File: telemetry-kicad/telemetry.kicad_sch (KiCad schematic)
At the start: 98 parts, among them J1 2601-1102, J2 RFPC-SMA27-F, J3 TC2030, J4 2601-1102, J5 2601-1102, J6 USB_C_Receptacle_USB2.0_16P, J7 SD_Card_Receptacle, Q1 DMP3099LQ-7, SW1 SW_NRST, SW2 SW_BOOT0, U1 LMR33610ADDAR, U10 TLC59108IPWR, U11 MCP1703T-5002E/CB, U2 ASM330LHHXG1TR, U3 MAX-M10S-00B, U4 TCAN337, U5 STM32H523RCT7, U6 TCAN337, U7 USBLC6-2SC6, U9 TLC59108IPWR, Y1 ABM8AIG-24.000MHz-8-2Z-T

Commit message: PCB draft complete
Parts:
- removed C28: 1uF, Capacitor_SMD:C_0805_2012Metric_Pad1.18x1.45mm_HandSolder, symbol Device:C
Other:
- moved on the sheet: C26, C27
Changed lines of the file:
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@@
 	(text "VDD (with bulk) and VDD_IO"
 		(exclude_from_sim no)
-		(at 130.048 257.302 0)
+		(at 130.048 258.572 0)
 		(effects
 			(font
@@
 	)
 	(junction
+		(at 139.7 252.73)
+		(diameter 0)
+		(color 0 0 0 0)
+	)
+	(junction
 		(at 57.15 41.91)
 		(diameter 0)
@@
 	)
 	(junction
-		(at 186.69 252.73)
+		(at 139.7 240.03)
 		(diameter 0)
 		(color 0 0 0 0)
 	)
 	(junction
-		(at 422.91 113.03)
+		(at 186.69 252.73)
 		(diameter 0)
 		(color 0 0 0 0)
 	)
 	(junction
-		(at 232.41 237.49)
+		(at 422.91 113.03)
 		(diameter 0)
 		(color 0 0 0 0)
 	)
 	(junction
-		(at 93.98 31.75)
+		(at 232.41 237.49)
 		(diameter 0)
 		(color 0 0 0 0)
 	)
 	(junction
-		(at 140.97 240.03)
+		(at 93.98 31.75)
 		(diameter 0)
 		(color 0 0 0 0)
@@
 	)
 	(junction
-		(at 140.97 252.73)
-		(diameter 0)
-		(color 0 0 0 0)
-	)
-	(junction
 		(at 186.69 240.03)
 		(diameter 0)
@@
 	(wire
 		(pts
-			(xy 153.67 240.03) (xy 153.67 242.57)
-		)
-		(stroke
-			(width 0)
-			(type default)
-		)
-	)
-	(wire
-		(pts
 			(xy 172.72 124.46) (xy 172.72 119.38)
 		)
@@
 	(wire
 		(pts
-			(xy 140.97 237.49) (xy 140.97 240.03)
+			(xy 139.7 238.76) (xy 139.7 240.03)
 		)
 		(stroke
@@
 	(wire
 		(pts
-			(xy 140.97 250.19) (xy 140.97 252.73)
+			(xy 146.05 250.19) (xy 146.05 252.73)
 		)
 		(stroke
@@
 	(wire
 		(pts
-			(xy 140.97 240.03) (xy 140.97 242.57)
-		)
-		(stroke
-			(width 0)
-			(type default)
-		)
-	)
-	(wire
-		(pts
-			(xy 153.67 252.73) (xy 153.67 250.19)
+			(xy 146.05 240.03) (xy 146.05 242.57)
 		)
 		(stroke
@@
 	(wire
 		(pts
-			(xy 140.97 240.03) (xy 153.67 240.03)
-		)
-		(stroke
-			(width 0)
-			(type default)
-		)
-	)
-	(wire
-		(pts
 			(xy 194.31 172.72) (xy 195.58 172.72)
 		)
@@
 	(wire
 		(pts
-			(xy 127 240.03) (xy 140.97 240.03)
+			(xy 132.08 240.03) (xy 139.7 240.03)
 		)
 		(stroke
@@
 	(wire
 		(pts
-			(xy 127 250.19) (xy 127 252.73)
+			(xy 132.08 250.19) (xy 132.08 252.73)
 		)
 		(stroke
@@
 	(wire
 		(pts
-			(xy 127 242.57) (xy 127 240.03)
+			(xy 132.08 242.57) (xy 132.08 240.03)
 		)
 		(stroke
@@
 	(wire
 		(pts
-			(xy 140.97 252.73) (xy 153.67 252.73)
-		)
-		(stroke
-			(width 0)
-			(type default)
-		)
-	)
-	(wire
-		(pts
 			(xy 124.46 114.3) (xy 123.19 114.3)
 		)
@@
 	(wire
 		(pts
+			(xy 139.7 240.03) (xy 146.05 240.03)
+		)
+		(stroke
+			(width 0)
+			(type default)
+		)
+	)
+	(wire
+		(pts
+			(xy 139.7 252.73) (xy 146.05 252.73)
+		)
+		(stroke
+			(width 0)
+			(type default)
+		)
+	)
+	(wire
+		(pts
 			(xy 238.76 39.37) (xy 238.76 34.29)
 		)
@@
 	(wire
 		(pts
-			(xy 127 252.73) (xy 140.97 252.73)
+			(xy 132.08 252.73) (xy 139.7 252.73)
 		)
 		(stroke
@@
 	(wire
 		(pts
-			(xy 140.97 252.73) (xy 140.97 255.27)
+			(xy 139.7 252.73) (xy 139.7 254)
 		)
 		(stroke
@@
 	(symbol
 		(lib_id "Device:C")
-		(at 140.97 246.38 0)
+		(at 146.05 246.38 0)
 		(unit 1)
 		(body_style 1)
@@
 		(fields_autoplaced yes)
 		(property "Reference" "C27"
-			(at 144.78 245.1099 0)
+			(at 149.86 245.1099 0)
 			(show_name no)
 			(do_not_autoplace no)
@@
 		)
 		(property "Value" "1uF"
-			(at 144.78 247.6499 0)
+			(at 149.86 247.6499 0)
 			(show_name no)
 			(do_not_autoplace no)
@@
 		)
 		(property "Footprint" "Capacitor_SMD:C_0805_2012Metric_Pad1.18x1.45mm_HandSolder"
-			(at 141.9352 250.19 0)
+			(at 147.0152 250.19 0)
 			(hide yes)
 			(show_name no)
@@
 		)
 		(property "Datasheet" ""
-			(at 140.97 246.38 0)
+			(at 146.05 246.38 0)
 			(hide yes)
 			(show_name no)
@@
 		)
 		(property "Description" "Unpolarized capacitor"
-			(at 140.97 246.38 0)
+			(at 146.05 246.38 0)
 			(hide yes)
 			(show_name no)
@@
 	(symbol
 		(lib_id "power:+3.3V")
-		(at 140.97 237.49 0)
+		(at 139.7 238.76 0)
 		(unit 1)
 		(body_style 1)
@@
 		(fields_autoplaced yes)
 		(property "Reference" "#PWR076"
-			(at 140.97 241.3 0)
+			(at 139.7 242.57 0)
 			(hide yes)
 			(show_name no)
@@
 		)
 		(property "Value" "+3.3V"
-			(at 140.97 232.41 0)
+			(at 139.7 233.68 0)
 			(show_name no)
 			(do_not_autoplace no)
@@
 		)
 		(property "Footprint" ""
-			(at 140.97 237.49 0)
+			(at 139.7 238.76 0)
 			(hide yes)
 			(show_name no)
@@
 		)
 		(property "Datasheet" ""
-			(at 140.97 237.49 0)
+			(at 139.7 238.76 0)
 			(hide yes)
 			(show_name no)
@@
 		)
 		(property "Description" "Power symbol creates a global label with name \"+3.3V\""
-			(at 140.97 237.49 0)
+			(at 139.7 238.76 0)
 			(hide yes)
 			(show_name no)
@@
 	(symbol
 		(lib_id "Device:C")
-		(at 127 246.38 180)
+		(at 132.08 246.38 180)
 		(unit 1)
 		(body_style 1)
@@
 		(fields_autoplaced yes)
 		(property "Reference" "C26"
-			(at 130.81 245.1099 0)
+			(at 135.89 245.1099 0)
 			(show_name no)
 			(do_not_autoplace no)
@@
 		)
 		(property "Value" "10uF"
-			(at 130.81 247.6499 0)
+			(at 135.89 247.6499 0)
 			(show_name no)
 			(do_not_autoplace no)
@@
 		)
 		(property "Footprint" "Capacitor_SMD:C_0805_2012Metric_Pad1.18x1.45mm_HandSolder"
-			(at 126.0348 242.57 0)
+			(at 131.1148 242.57 0)
 			(hide yes)
 			(show_name no)
@@
 		)
 		(property "Datasheet" ""
-			(at 127 246.38 0)
+			(at 132.08 246.38 0)
 			(hide yes)
 			(show_name no)
@@
 		)
 		(property "Description" "Unpolarized capacitor"
-			(at 127 246.38 0)
+			(at 132.08 246.38 0)
 			(hide yes)
 			(show_name no)
@@
 	(symbol
 		(lib_id "power:GND")
-		(at 140.97 255.27 0)
+		(at 139.7 254 0)
 		(unit 1)
 		(body_style 1)
@@
 		(fields_autoplaced yes)
 		(property "Reference" "#PWR081"
-			(at 140.97 261.62 0)
+			(at 139.7 260.35 0)
 			(hide yes)
 			(show_name no)
@@
 		)
 		(property "Value" "GND"
-			(at 140.97 260.35 0)
+			(at 139.7 259.08 0)
 			(hide yes)
 			(show_name no)
@@
 		)
 		(property "Footprint" ""
-			(at 140.97 255.27 0)
+			(at 139.7 254 0)
 			(hide yes)
 			(show_name no)
@@
 		)
 		(property "Datasheet" ""
-			(at 140.97 255.27 0)
+			(at 139.7 254 0)
 			(hide yes)
 			(show_name no)
@@
 		)
 		(property "Description" "Power symbol creates a global label with name \"GND\" , ground"
-			(at 140.97 255.27 0)
+			(at 139.7 254 0)
 			(hide yes)
 			(show_name no)
@@
 					(unit 1)
 				)
-			)
-		)
-	)
-	(symbol
-		(lib_id "Device:C")
-		(at 153.67 246.38 0)
-		(unit 1)
-		(body_style 1)
-		(exclude_from_sim no)
-		(in_bom yes)
-		(on_board yes)
-		(in_pos_files yes)
-		(dnp no)
-		(fields_autoplaced yes)
-		(property "Reference" "C28"
-			(at 157.48 245.1099 0)
-			(show_name no)
-			(do_not_autoplace no)
-			(effects
-				(font
-					(size 1.27 1.27)
-				)
-				(justify left)
-			)
-		)
-		(property "Value" "1uF"
-			(at 157.48 247.6499 0)
-			(show_name no)
-			(do_not_autoplace no)
-			(effects
-				(font
-					(size 1.27 1.27)
-				)
-				(justify left)
-			)
-		)
-		(property "Footprint" "Capacitor_SMD:C_0805_2012Metric_Pad1.18x1.45mm_HandSolder"
-			(at 154.6352 250.19 0)
-			(hide yes)
-			(show_name no)
-			(do_not_autoplace no)
-			(effects
-				(font
-					(size 1.27 1.27)
-				)
-			)
-		)
-		(property "Datasheet" ""
-			(at 153.67 246.38 0)
-			(hide yes)
-			(show_name no)
-			(do_not_autoplace no)
-			(effects
-				(font
-					(size 1.27 1.27)
-				)
-			)
-		)
-		(property "Description" "Unpolarized capacitor"
-			(at 153.67 246.38 0)
-			(hide yes)
-			(show_name no)
-			(do_not_autoplace no)
-			(effects
-				(font
-					(size 1.27 1.27)
-				)
-			)
-		)
-		(pin "1"
-		)
-		(pin "2"
-		)
-		(instances
-			(project "telemetry"
-				(path "/3df6834d-aaf5-42e5-8a41-0f444a5b1186"
-					(reference "C28")
-					(unit 1)
-				)

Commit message: Changed ublox MAX-M10 to Quectel LC29HBAMD to enable the option of using RTK as well as keeping the dead reckoning features
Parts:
- removed U3: MAX-M10S-00B, telemetry:MAX-M10S-00B, symbol telemetry:MAX-M10S-00B
- added R22: 10K, Resistor_SMD:R_0805_2012Metric_Pad1.20x1.40mm_HandSolder, symbol Device:R_US
- added R23: 39k, LC29HBAMD, symbol Device:R_US
- added SW3: CJS-1200TB1, bspd:CJS-1200TB1, symbol telemetry:CJS-1200TB1
- added U3: LC29HBAMD, LC29HBAMD, symbol telemetry:LC29HBAMD
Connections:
- net +3.3V: now also C33.2, C34.2, U10.20 (VCC), U9.20 (VCC), R22.1, U3.22 (V_BCKP), U3.23 (VCC)
- net +5V: no longer C33.2, C34.2, U10.20 (VCC), U9.20 (VCC)
- net ANT: now also U3.11 (RF_IN)
- net CS_IMU: now also R22.2
- net GND: now also U3.10 (GND), U3.12 (GND), U3.13 (GND), U3.24 (GND)
- net RXD_CAN2: now also U5.33 (PB12); no longer U5.34 (PB13)
- net TXD_CAN2: now also U5.34 (PB13); no longer U5.33 (PB12)
- net VBUS_USB: now also C32.2, D6.1 (K), U11.3 (VIN)
- net V_IN: no longer C32.2, D6.1 (K), U11.3 (VIN)
- net RXD_GNSS: no longer names the net of U5.35 (PB14)
- net TXD_GNSS: no longer names the net of U5.36 (PB15)
- new net: R23.1, U3.7 (VDD_EXT)
- new net: R23.2, U3.5 (D_SEL1)
- new net CLK_GNSS: U3.19 (I2C_SCL/SPI_CLK)
- new net CS_GNSS: U3.18 (I2C_SDA/SPI_CS)
- new net MISO_GNSS: U3.20 (TXD1/SPI_MISO)
- new net MOSI_GNSS: U3.21 (RXD1/SPI_MOSI)
- new net RESET_GNSS: U3.8 (RESET_IN)
- new net TIMERIN_GNSS: U3.3 (1PPS)
- no-connect marks 13 -> 5
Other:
- note added: "Level shifting required for a bunch of things"
- moved on the sheet: C11, J2

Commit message: update
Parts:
- R23, U3: footprint LC29HBAMD -> (none)
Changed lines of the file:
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@@
 			)
 		)
-		(property "Footprint" "LC29HBAMD"
+		(property "Footprint" ""
 			(at 29.464 89.154 90)
 			(hide yes)
@@
 			)
 		)
-		(property "Footprint" "LC29HBAMD"
+		(property "Footprint" ""
 			(at 40.64 74.93 0)
 			(hide yes)

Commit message: Added 12V/USB_5V power mux and level shifting for GNSS module
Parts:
- added C28, C36, C38: 100nF, Capacitor_SMD:C_0805_2012Metric_Pad1.18x1.45mm_HandSolder, symbol Device:C
- added C37: 10uF, Capacitor_SMD:C_0805_2012Metric_Pad1.18x1.45mm_HandSolder, symbol Device:C
- added C39: 1uF, Capacitor_SMD:C_0805_2012Metric_Pad1.18x1.45mm_HandSolder, symbol Device:C
- added R24: 10k, Resistor_SMD:R_0805_2012Metric_Pad1.20x1.40mm_HandSolder, symbol Device:R_US
- added R25, R26, R29, R30: R_US, Resistor_THT:R_Array_SIP4, symbol Device:R_US
- added R31: 21.5k, Resistor_THT:R_Array_SIP4, symbol Device:R_US
- added U13: TXS0108EPW, Package_SO:TSSOP-20_4.4x6.5mm_P0.65mm, symbol Logic_LevelTranslator:TXS0108EPW
- added U8: TPS2121RUXR, telemetry:VQFN-HR-12_L2.5-W2.0-P0.50-BL, symbol telemetry:TPS2121RUXR
- U3: footprint (none) -> LC29HBAMD
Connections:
- net TIMEPULSE_GNSS is gone; now on net RESET_GNSS: U5.37 (PC6)
- net +3.3V: now also U3.9 (VDD_RF), C28.1, C37.1, C38.2, U13.19 (VCCB)
- net CLK_GNSS: now also U5.16 (PA2), U13.17 (B3); no longer U3.19 (I2C_SCL/SPI_CLK)
- net CS_GNSS: now also U5.17 (PA3), U13.16 (B4); no longer U3.18 (I2C_SDA/SPI_CS)
- net GND: now also SW3.2 (B), C28.2, C36.1, C37.2, C38.1, C39.2, R24.1, R26.2, R30.2, R31.2, U13.11 (GND), U8.12 (GND), U8.9 (ST)
- net MISO_GNSS: now also U5.15 (PA1), U13.18 (B2); no longer U3.20 (TXD1/SPI_MISO)
- net MOSI_GNSS: now also U5.14 (PA0), U13.20 (B1); no longer U3.21 (RXD1/SPI_MOSI)
- net RESET_GNSS: now also U13.14 (B6); no longer U3.8 (RESET_IN)
- net TIMERIN_GNSS: now also U5.42 (PA9), U13.15 (B5); no longer U3.3 (1PPS)
- net VBUS_USB: now also R25.1, U8.2 (IN2)
- net V_IN: now also U8.1 (OUT), U8.8 (OUT); no longer J1.1 (1_1), J1.2 (1_2)
- net VDD_EXT: now reaches R23.1, U3.7 (VDD_EXT)
- net VDD_EXT: now also C36.2, R24.2, U13.10 (OE), U13.2 (VCCA)
- net SW_B: now reaches SW3.1 (A)
- net SW_B: now also U5.9 (PC1)
- net SW_A: now reaches SW3.3 (C)
- net SW_A: now also U5.8 (PC0)
- new net: R31.1, U8.10 (ILM)
- new net: C39.1, U8.11 (SS)
- new net +12V: J1.1 (1_1), J1.2 (1_2), R29.1, U8.7 (IN1)
- new net CLK_GNSS_1.8V: U13.4 (A3), U3.19 (I2C_SCL/SPI_CLK)
- new net CS_GNSS_1.8V: U13.5 (A4), U3.18 (I2C_SDA/SPI_CS)
- new net DIV1_MUX: R29.2, R30.1, U8.5 (OV1), U8.6 (PR1)
- new net DIV2_MUX: R25.2, R26.1, U8.3 (CP2), U8.4 (OV2)
- new net MISO_GNSS_1.8V: U13.3 (A2), U3.20 (TXD1/SPI_MISO)
- new net MOSI_GNSS_1.8V: U13.1 (A1), U3.21 (RXD1/SPI_MOSI)
- new net RESET_GNSS_1.8V: U13.7 (A6), U3.8 (RESET_IN)
- new net TIMERIN_GNSS_1.8V: U13.6 (A5), U3.3 (1PPS)
- no-connect marks 5 -> 12
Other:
- note added: "Figure out 12V"
- note added: "Power Mux"
- note added: "To do: - Power in from Car, need to figure out power"
- note removed: "Level shifting required for a bunch of things"
- note removed: "To do: - LEDs configuration, same brightness - CAN termination? - Consider deutch terminals instead of wago - Check FET operation with 5V"
- moved on the sheet: C17, J7, R14, R15, R16, R17, R18, R19, SW3

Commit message: small fixes
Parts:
- added SW4: CJS-1200TB1, telemetry:CJS-1200TB1, symbol telemetry:CJS-1200TB1
- C1, C10, C11, C12, C13, C14, C15, C16, C17, C18, C19, C2, C20, C21, C22, C23, C24, C25, C26, C27, C28, C29, C3, C30, C31, C32, C33, C34, C35, C36, C37, C38, C39, C4, C5, C6, C7, C8, C9: footprint Capacitor_SMD:C_0805_2012Metric_Pad1.18x1.45mm_HandSolder -> Capacitor_SMD:C_0402_1005Metric_Pad0.74x0.62mm_HandSolder
- LED1, LED2, LED3, LED4, LED5: footprint telemetry:LED-SMD_4P-L2.0-W1.3-RD-TL -> telemetry:XL-2012SURUGC
- R1, R10, R11, R12, R13, R14, R15, R16, R17, R18, R19, R2, R20, R21, R22, R24, R3, R4, R5, R6, R7, R8, R9: footprint Resistor_SMD:R_0805_2012Metric_Pad1.20x1.40mm_HandSolder -> Resistor_SMD:R_0402_1005Metric_Pad0.72x0.64mm_HandSolder
- R23: footprint (none) -> Resistor_SMD:R_0402_1005Metric_Pad0.72x0.64mm_HandSolder
- R25, R31: footprint Resistor_THT:R_Array_SIP4 -> Resistor_SMD:R_0402_1005Metric_Pad0.72x0.64mm_HandSolder
- R26, R30: value R_US -> 5k; footprint Resistor_THT:R_Array_SIP4 -> Resistor_SMD:R_0402_1005Metric_Pad0.72x0.64mm_HandSolder
- R27: value 1.1k -> 1.87k; footprint Resistor_SMD:R_0805_2012Metric_Pad1.20x1.40mm_HandSolder -> Resistor_SMD:R_0402_1005Metric_Pad0.72x0.64mm_HandSolder
- R28: value 3.74k -> 8.66k; footprint Resistor_SMD:R_0805_2012Metric_Pad1.20x1.40mm_HandSolder -> Resistor_SMD:R_0402_1005Metric_Pad0.72x0.64mm_HandSolder
- R29: value R_US -> 18.2k; footprint Resistor_THT:R_Array_SIP4 -> Resistor_SMD:R_0402_1005Metric_Pad0.72x0.64mm_HandSolder
- SW3: footprint bspd:CJS-1200TB1 -> telemetry:CJS-1200TB1
- U3: footprint LC29HBAMD -> telemetry:LC29HBAMD
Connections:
- net +12V: now also D6.1 (K)
- net GND: now also SW4.2 (B)
- net VBUS_USB: no longer C2.1, C3.1, C32.2, D1.1 (K), D6.1 (K), Q1.2 (S), TP1.1, U1.2 (VIN), U1.3 (EN), U11.3 (VIN)
- net SW_C: now reaches U5.10 (PC2)
- net SW_C: now also SW4.3 (C)
- net SW_D: now reaches U5.11 (PC3)
- net SW_D: now also SW4.1 (A)
- new net V_HV: C2.1, C3.1, C32.2, D1.1 (K), Q1.2 (S), TP1.1, U1.2 (VIN), U1.3 (EN), U11.3 (VIN)
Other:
- note added: "Check these resistors"
- note added: "Switch Inputs"
- note removed: "Figure out 12V"
- moved on the sheet: C39, R25, R26, R29, R30, R31, U8

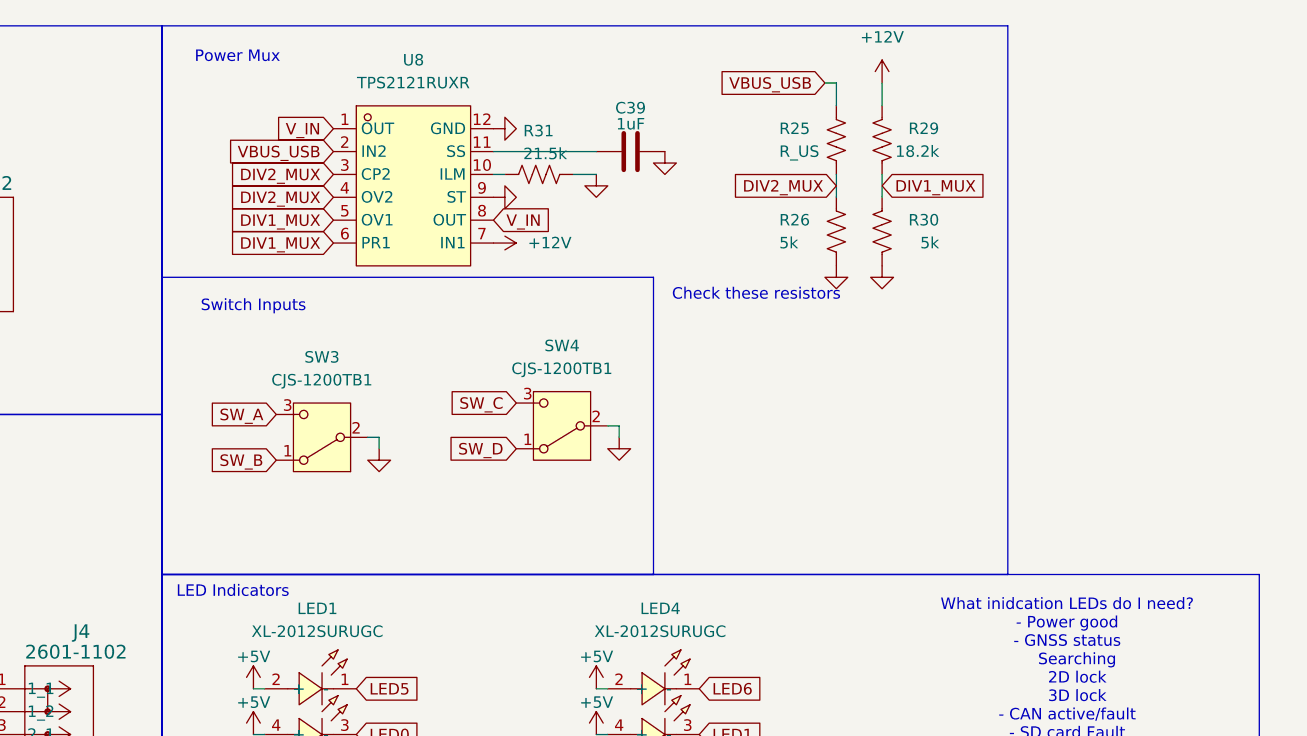
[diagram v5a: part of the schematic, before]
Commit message: Solved resistors for TPS2121 power mux operation
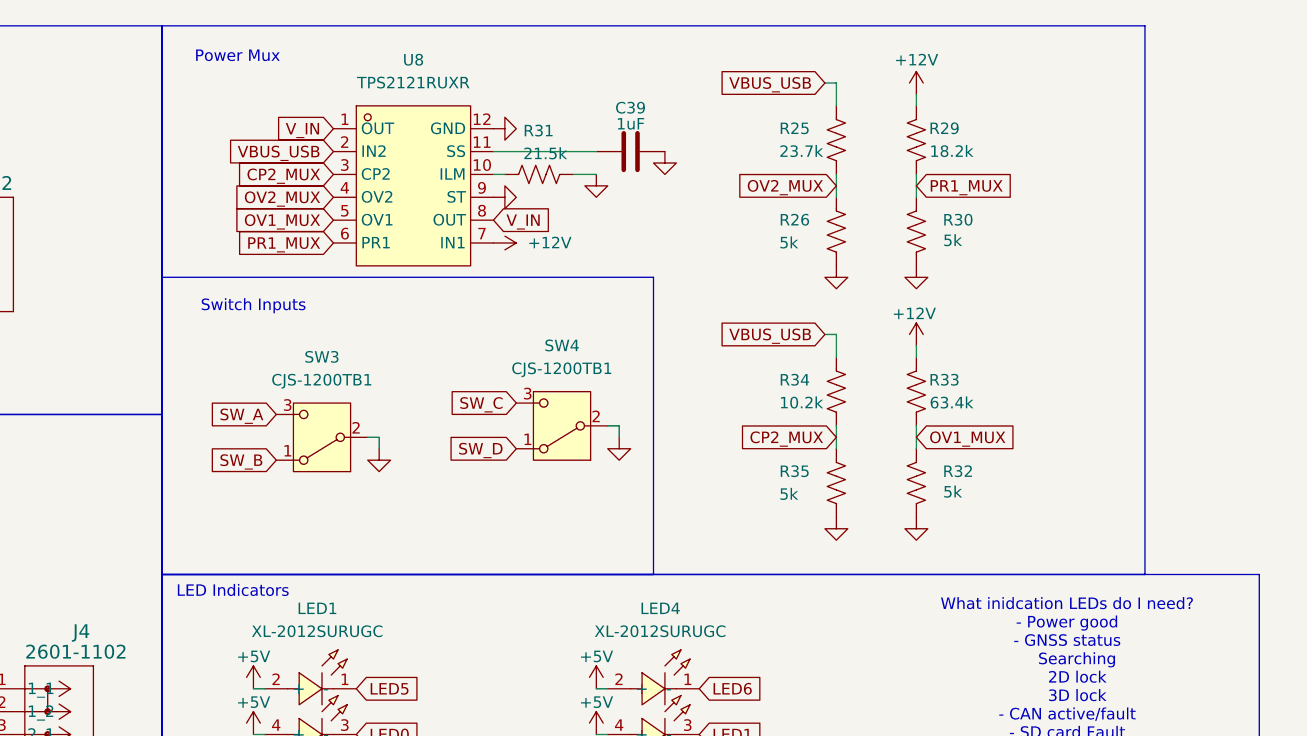
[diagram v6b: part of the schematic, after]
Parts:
- added R32, R35: 5k, Resistor_SMD:R_0402_1005Metric_Pad0.72x0.64mm_HandSolder, symbol Device:R_US
- added R33: 63.4k, Resistor_SMD:R_0402_1005Metric_Pad0.72x0.64mm_HandSolder, symbol Device:R_US
- added R34: 10.2k, Resistor_SMD:R_0402_1005Metric_Pad0.72x0.64mm_HandSolder, symbol Device:R_US
- R25: value R_US -> 23.7k
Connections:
- net +12V: now also R33.1
- net GND: now also R32.2, R35.2
- net VBUS_USB: now also R34.1
- net DIV1_MUX renamed PR1_MUX
- net PR1_MUX: no longer U8.5 (OV1)
- net DIV2_MUX renamed OV2_MUX
- net OV2_MUX: no longer U8.3 (CP2)
- new net CP2_MUX: R34.2, R35.1, U8.3 (CP2)
- new net OV1_MUX: R32.1, R33.2, U8.5 (OV1)
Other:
- note removed: "Check these resistors"
- moved on the sheet: R29, R30
